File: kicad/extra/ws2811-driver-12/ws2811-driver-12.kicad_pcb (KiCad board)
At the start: 2 copper layers, 140 x 25 mm, 17 parts, among them J1 Conn_01x13_Pin, J3 RJ45 IN, J4 RJ45 OUT, U1 WS2811, U2 WS2811, U3 WS2811, U4 WS2811

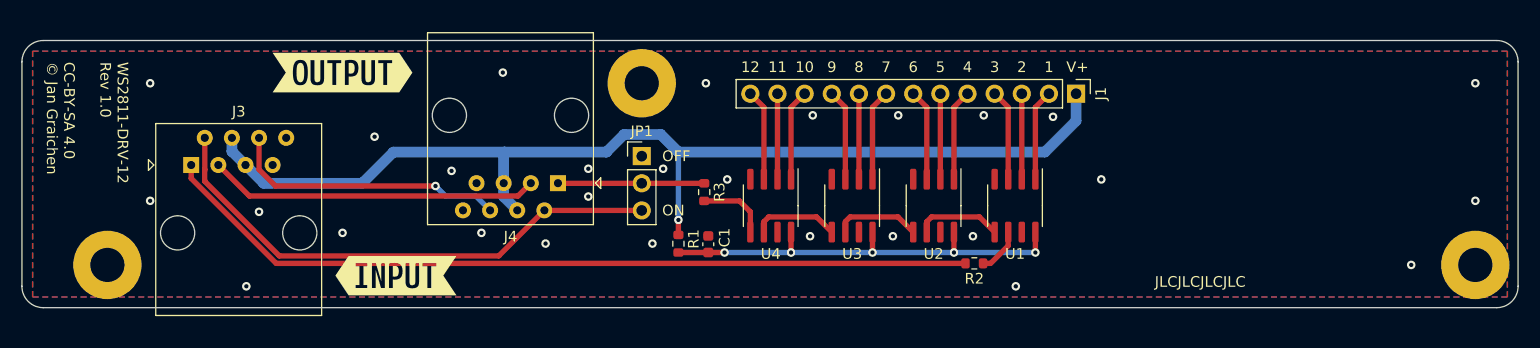
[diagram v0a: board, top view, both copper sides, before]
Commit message: feat: Rework WS2811 boards (Rev 2.0)
* Change RJ45 pinout: The data signal is always paired with a ground
  line to increase signal stability, and the changed wireing eases the
  traces on the boards.

* All WS2811 driver boards have a three pin header for direct drive now.
  They can be directly connected to a signal decoder, e.g. for testing.

* The adapter boards has jumper pins to bypass RJ45 jacks, in case you
  want to connect another board using the final pin header.

* Change pin header component to a better available JCSC parts number.

* Move RJ45 jacks on driver boards a bit more off the board, so that
  there is less space between the jack and the outer side of the Watti
  carrier. This makes it easier to plug in and out RJ45 cables as
  the latches are easier to reach.

Fixes #4
Fixes #5
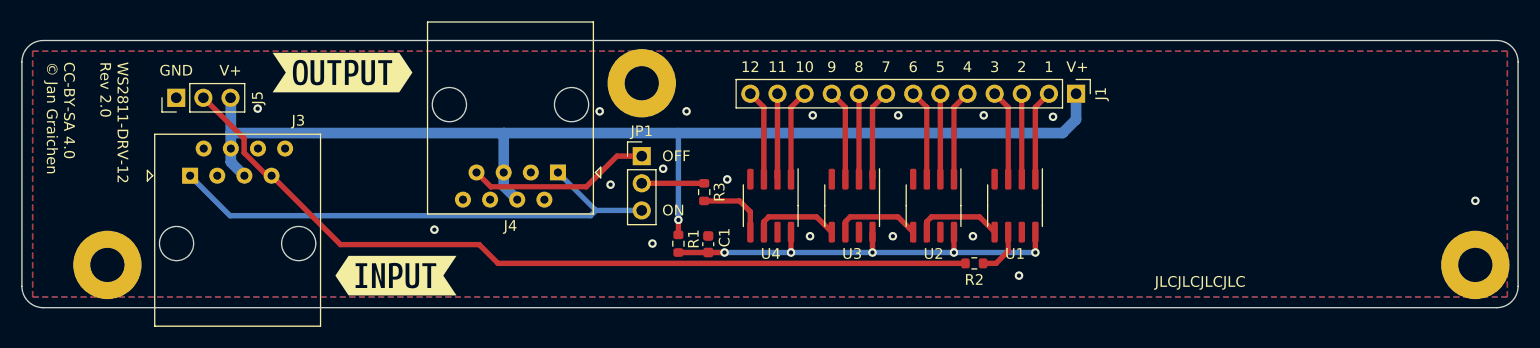
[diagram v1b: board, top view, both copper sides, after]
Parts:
- added J5: Conn_01x03_Pin, Connector_PinHeader_2.54mm:PinHeader_1x03_P2.54mm_Vertical, F.Cu at (91.4, 86.4)
- moved J3 1.00 mm to (92.7, 93.7)
- moved J4 1.00 mm to (127.2, 93.3)
- turned R2 to 0 degrees
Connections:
- J3 pad 1: Net-(J3-Pad1) -> Net-(JP1-B)
- J3 pad 2: Net-(JP1-B) -> GND
- J3 pad 3: Net-(J3-Pad3) -> GND
- J3 pad 6: Net-(J3-Pad6) -> GND
- J3 pad 7: GND -> Net-(J5-Pin_2)
- J4 pad 1: Net-(JP1-C) -> Net-(JP1-B)
- J4 pad 2: Net-(JP1-B) -> GND
- J4 pad 3: Net-(J3-Pad3) -> GND
- J4 pad 6: Net-(J3-Pad6) -> GND
- J4 pad 7: GND -> Net-(JP1-A)
- JP1 pad 1: unconnected-(JP1-A-Pad1) -> Net-(JP1-A)
- R2 pad 1: Net-(U1-DIN) -> Net-(J5-Pin_2)
- R2 pad 2: Net-(J3-Pad1) -> Net-(U1-DIN)
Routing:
- net Net-(J5-Pin_2): track 0.00 -> 78.5 mm
- net Net-(J3-Pad1): track 77.0 -> 0.00 mm
- net Net-(J3-Pad3): track 30.9 -> 0.00 mm
- net Net-(J3-Pad6): track 26.2 -> 0.00 mm, vias 1 -> 0
- net Net-(JP1-A): track 0.00 -> 17.2 mm
- net Net-(JP1-C): track 13.7 -> 5.84 mm
- net VCC: track 101.6 -> 106.1 mm
- net Net-(JP1-B): track 49.6 -> 49.0 mm
- net GND: vias 28 -> 17
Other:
- board text added: "GND"
- board text added: "WS2811-DRV-12 Rev ${REVISION}"
- board text removed: "WS2811-DRV-12 Rev 1.0"
